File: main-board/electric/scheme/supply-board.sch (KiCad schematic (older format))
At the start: 139 parts, among them K1 CONN_3, P1 PWR-IN, P10 TST, P11 TST, P12 PWR-IN, P13 CONN_4, P14 PWR-IN, P16 TST, P17 TST, P18 TST, P19 TST, P2 PWR-IN, P3 CONN_4, P4 cross board conn, P5 PWR-IN, P6 TST, P7 TST, P8 TST, P9 CONN_3X2, Q1 BC847, Q10 MOS_N, Q11 MOS_P, Q12 MOS_P, Q2 BC847, Q3 BC847, Q4 MOS_P, Q5 BC847, Q6 BC857, Q7 BC847, Q8 BC857, Q9 BC847, U1 NCP3063, U2 L293, U3 MINI-USB-B, X1 8MHz

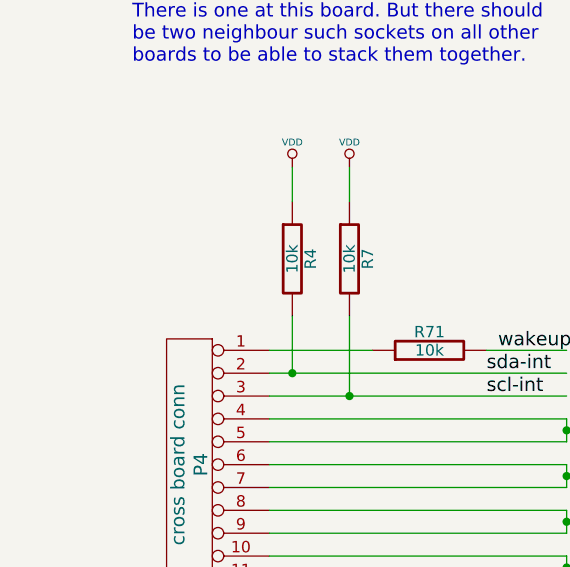
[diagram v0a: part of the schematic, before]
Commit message: Placing elements.
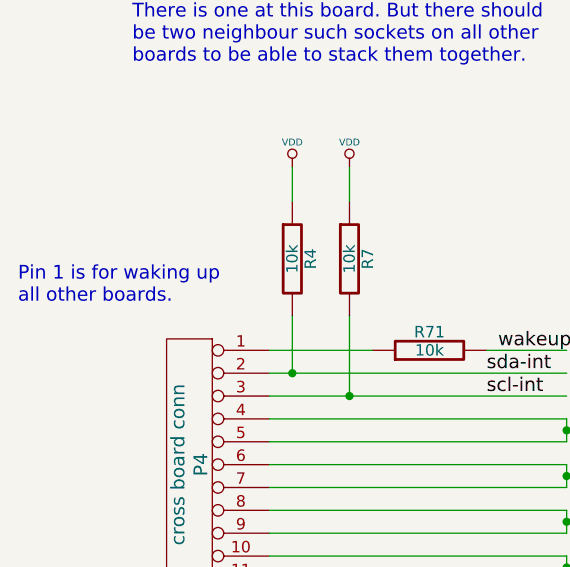
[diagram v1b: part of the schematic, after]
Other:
- note added: "Pin 1 is for waking up \nall other boards."

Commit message: Changed USB power from "batt+" to "solar+".
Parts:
- removed P17, P18, P19: TST, ~, symbol TST
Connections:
- no-connect marks 12 -> 9
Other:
- note added: "Optionally could be USB powered \nthrough "solar+". It is because of \nability to control current through \n"solar+"."
- note removed: "Optionally could be USB powered"
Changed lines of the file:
@@
 Sheet 1 1
 Title ""
-Date "25 aug 2013"
+Date "26 aug 2013"
 Rev ""
 Comp ""
@@
 	29850 18500 29850 17850
 Text Label 29850 18100 1    60   ~ 0
-batt+
-Text Notes 28900 17750 0    60   ~ 0
-Optionally could be USB powered
+solar+
+Text Notes 28850 17500 0    60   ~ 0
+Optionally could be USB powered \nthrough "solar+". It is because of \nability to control current through \n"solar+".
 Text Notes 13550 13400 0    60   ~ 0
 This capacitor gives cutoff frequency at about 170kHz.
@@
 $EndComp
 NoConn ~ 3700 5650
-$Comp
-L TST P17
-U 1 1 5214C655
-P 3950 5650
-F 0 "P17" H 3950 5950 40  0000 C CNN
-F 1 "TST" H 3950 5900 30  0000 C CNN
-F 2 "~" H 3950 5650 60  0000 C CNN
-F 3 "~" H 3950 5650 60  0000 C CNN
-	1    3950 5650
-	1    0    0    -1
-$EndComp
-NoConn ~ 3950 5650
-$Comp
-L TST P18
-U 1 1 5214C65C
-P 4200 5650
-F 0 "P18" H 4200 5950 40  0000 C CNN
-F 1 "TST" H 4200 5900 30  0000 C CNN
-F 2 "~" H 4200 5650 60  0000 C CNN
-F 3 "~" H 4200 5650 60  0000 C CNN
-	1    4200 5650
-	1    0    0    -1
-$EndComp
-NoConn ~ 4200 5650
-$Comp
-L TST P19
-U 1 1 5214C663
-P 4450 5650
-F 0 "P19" H 4450 5950 40  0000 C CNN
-F 1 "TST" H 4450 5900 30  0000 C CNN
-F 2 "~" H 4450 5650 60  0000 C CNN
-F 3 "~" H 4450 5650 60  0000 C CNN
-	1    4450 5650
-	1    0    0    -1
-$EndComp
-NoConn ~ 4450 5650
 Text Notes 3450 5250 0    60   ~ 0
 And four for screws at board corners.

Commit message: Routing...
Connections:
- no-connect marks 9 -> 8
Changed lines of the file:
@@
 Sheet 1 1
 Title ""
-Date "26 aug 2013"
+Date "29 aug 2013"
 Rev ""
 Comp ""
@@
 	1    0    0    -1
 $EndComp
-Text Label 14000 9550 0    60   ~ 0
+Text Label 8400 6350 0    60   ~ 0
 moto4
-Text Label 14000 9750 0    60   ~ 0
+Text Label 8400 7050 0    60   ~ 0
 moto3
 Text Label 13950 8750 0    60   ~ 0
@@
 	1    0    0    -1
 $EndComp
-Text Label 14100 9350 0    60   ~ 0
+Text Label 13950 7950 0    60   ~ 0
 light
 Text Label 23950 16300 0    60   ~ 0
@@
 	0    -1   -1   0
 $EndComp
-Text Label 8400 6350 0    60   ~ 0
+Text Label 14100 9550 0    60   ~ 0
 led1
 Text Label 13950 9150 0    60   ~ 0
@@
 Wire Wire Line
 	9050 7050 8350 7050
-Text Label 8400 7050 0    60   ~ 0
+Text Label 14100 9750 0    60   ~ 0
 led2
-Wire Wire Line
-	13650 6450 14350 6450
-Text Label 14000 6450 0    60   ~ 0
+Text Label 14100 4650 0    60   ~ 0
 usb-connected
 Text Label 14400 5250 0    60   ~ 0
@@
 rx
 NoConn ~ 14500 3050
-NoConn ~ 14500 4650
 $Comp
 L CONN_2 P14
@@
 Text Label 2700 7300 0    60   ~ 0
 wakeup
-NoConn ~ 13650 7950
 Wire Wire Line
 	13650 7600 14300 7600
@@
 Text Notes 600  7100 0    60   ~ 0
 Pin 1 is for waking up \nall other boards.
+NoConn ~ 13650 6450
+Wire Wire Line
+	13650 7950 14300 7950
 $EndSCHEMATC

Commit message: Routing and changing netlist to make routing more convenient.
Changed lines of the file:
@@
 Sheet 1 1
 Title ""
-Date "29 aug 2013"
+Date "30 aug 2013"
 Rev ""
 Comp ""
@@
 Text Label 8400 7050 0    60   ~ 0
 moto3
+Text Label 13950 8550 0    60   ~ 0
+moto2
 Text Label 13950 8750 0    60   ~ 0
-moto2
-Text Label 13950 8550 0    60   ~ 0
 moto1
 Text Label 14100 2750 0    60   ~ 0
@@
 Text Label 22350 12500 0    60   ~ 0
 moto-en
+Text Label 27550 13100 0    60   ~ 0
+out4
+Text Label 27550 13200 0    60   ~ 0
+out3
+Text Label 27550 13400 0    60   ~ 0
+out2
 Text Label 27550 13300 0    60   ~ 0
-out4
-Text Label 27550 13400 0    60   ~ 0
-out3
-Text Label 27550 13100 0    60   ~ 0
-out2
-Text Label 27550 13200 0    60   ~ 0
 out1
 $Comp

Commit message: Routing...
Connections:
- wire segments 412 -> 411
- no-connect marks 8 -> 9
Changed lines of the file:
@@
 Text Label 14000 3250 0    60   ~ 0
 boost-pwm
-Text Label 14100 4050 0    60   ~ 0
+Text Label 14000 3850 0    60   ~ 0
 buck-volt
-Text Label 14100 3850 0    60   ~ 0
+Text Label 14000 3650 0    60   ~ 0
 batt-volt
-Text Label 14100 3650 0    60   ~ 0
+Text Label 14000 4050 0    60   ~ 0
 solar-volt
 Text Label 24150 6550 1    60   ~ 0
@@
 	2450 5000 2900 5000
 Wire Wire Line
-	2900 5100 2450 5100
-Wire Wire Line
 	1650 5100 1150 5100
 Wire Wire Line
@@
 Wire Wire Line
 	2900 5200 2900 5300
-Wire Wire Line
-	2900 4700 2900 5100
-Connection ~ 2900 5000
 Text Label 2100 20950 1    60   ~ 0
 batt+
@@
 Wire Wire Line
 	13650 7950 14300 7950
+Wire Wire Line
+	2900 5000 2900 4350
+NoConn ~ 2450 5100
 $EndSCHEMATC

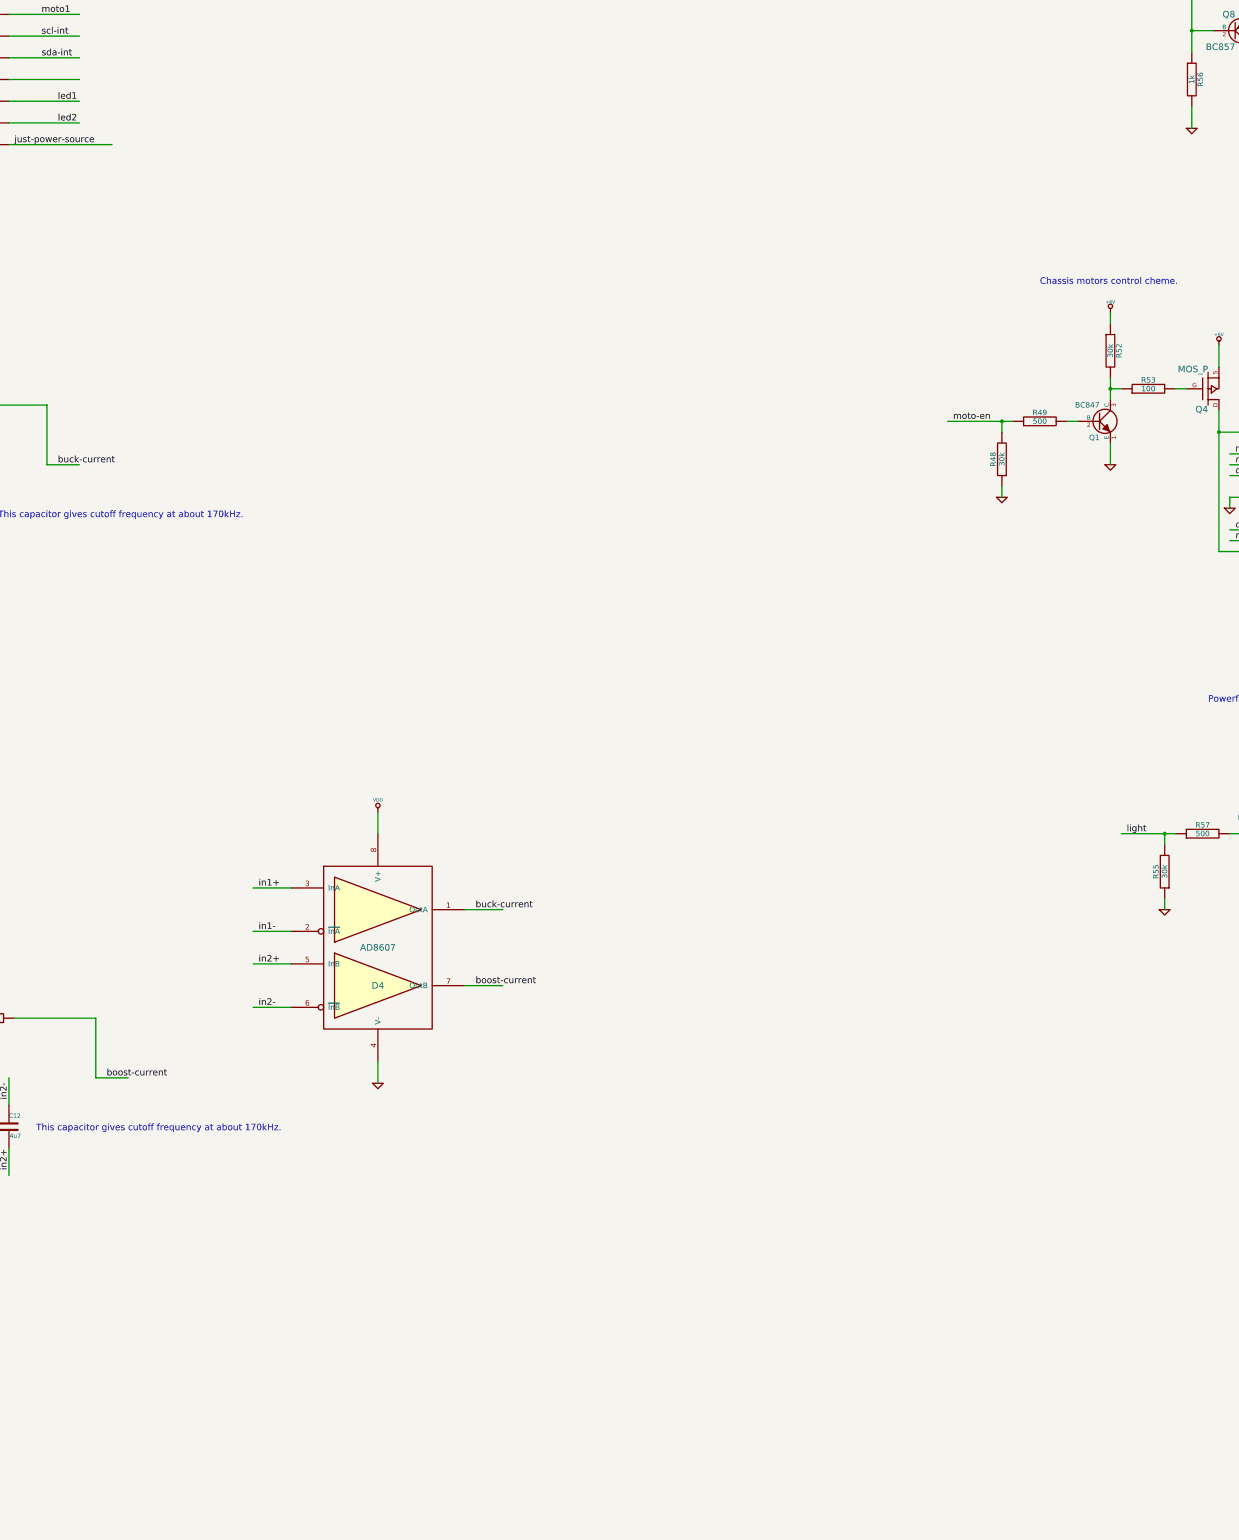
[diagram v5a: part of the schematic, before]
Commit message: Added acelerometer (it's optional).
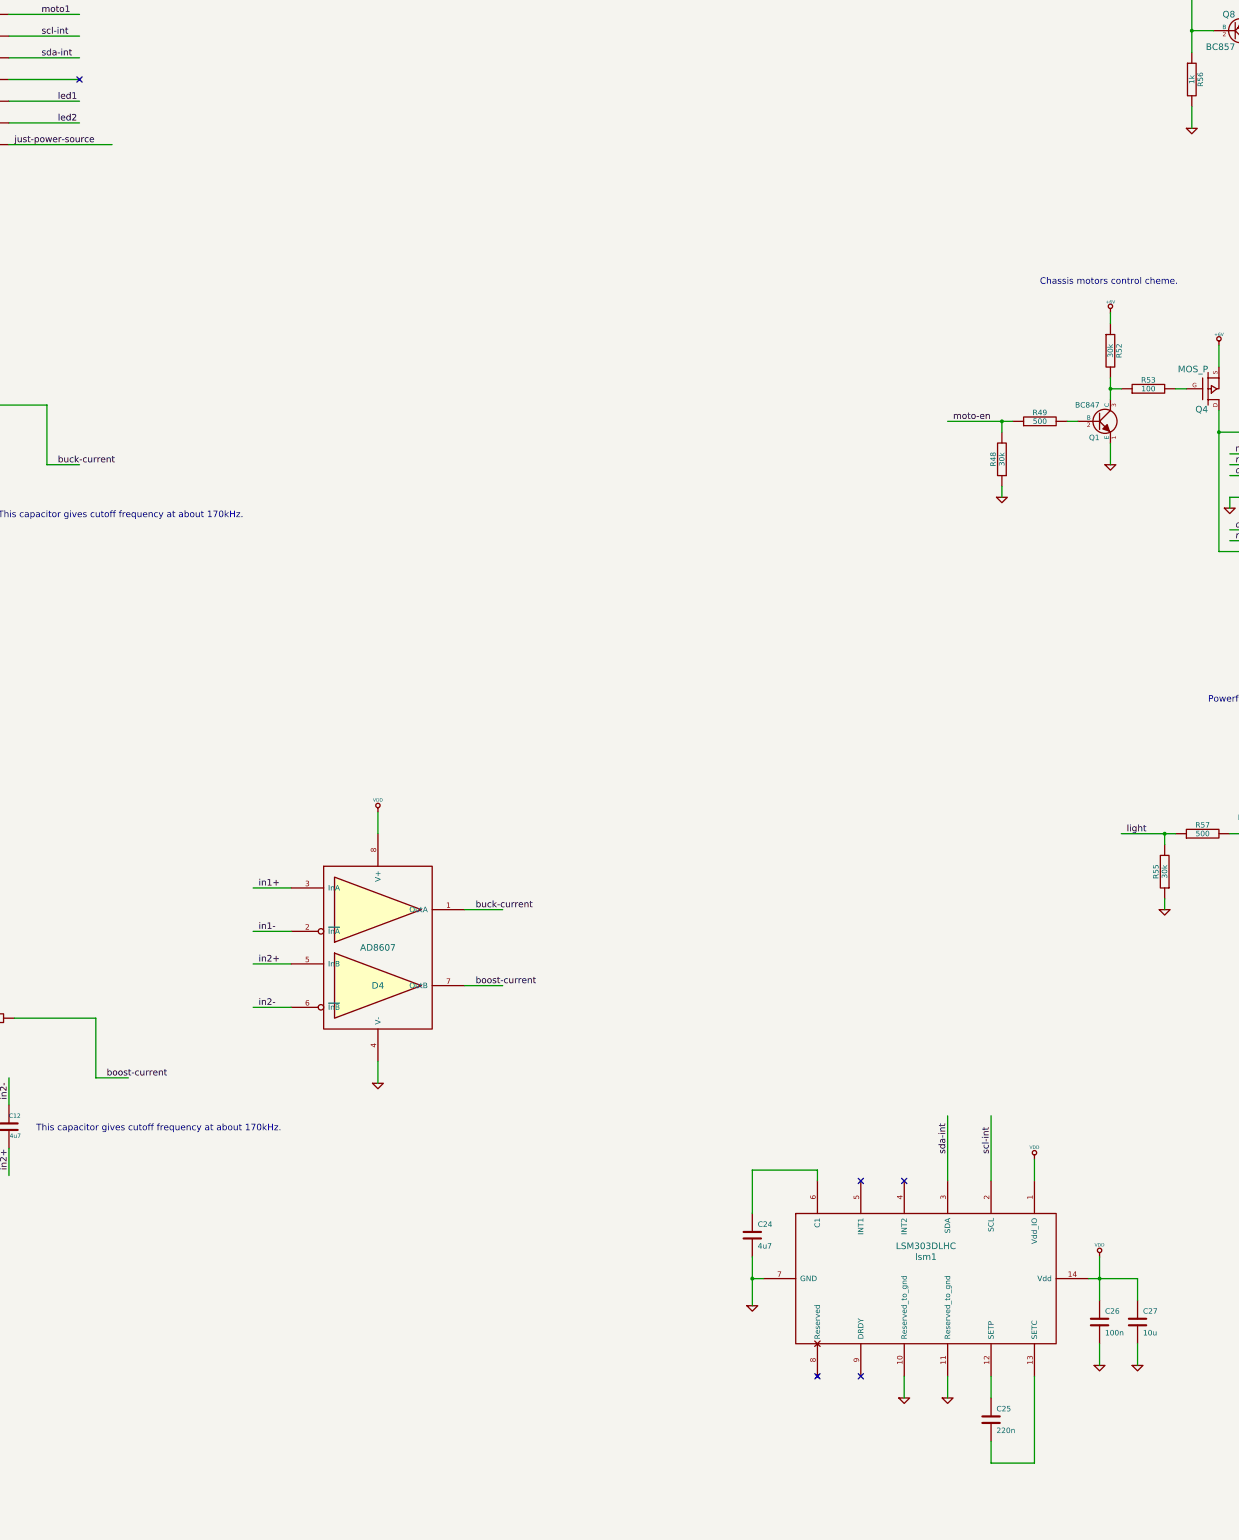
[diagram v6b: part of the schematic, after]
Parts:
- added C24: 4u7, symbol C
- added C25: 220n, symbol C
- added C26: 100n, symbol C
- added C27: 10u, symbol C
- added lsm1: LSM303DLHC, symbol LSM303DLHC
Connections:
- wire segments 411 -> 430
- no-connect marks 9 -> 14
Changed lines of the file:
@@
 Sheet 1 1
 Title ""
-Date "30 aug 2013"
+Date "31 aug 2013"
 Rev ""
 Comp ""
@@
 	2900 5000 2900 4350
 NoConn ~ 2450 5100
+Wire Wire Line
+	22300 19500 22300 18900
+Wire Wire Line
+	24050 21000 24050 21200
+Connection ~ 23700 20400
+Wire Wire Line
+	23600 20400 24050 20400
+Wire Wire Line
+	24050 20400 24050 20600
+Wire Wire Line
+	23100 19500 23100 19300
+Wire Wire Line
+	22700 21300 22700 21500
+Connection ~ 20500 20400
+Wire Wire Line
+	20500 20650 20500 20200
+Wire Wire Line
+	20500 19800 20500 19400
+Wire Wire Line
+	20500 19400 21100 19400
+Wire Wire Line
+	21100 19400 21100 19500
+Wire Wire Line
+	20500 20400 20600 20400
+Wire Wire Line
+	22300 21300 22300 21500
+Wire Wire Line
+	21900 21300 21900 21500
+Wire Wire Line
+	22700 21900 22700 22100
+Wire Wire Line
+	22700 22100 23100 22100
+Wire Wire Line
+	23100 22100 23100 21300
+Wire Wire Line
+	23700 21000 23700 21200
+Wire Wire Line
+	23700 20200 23700 20600
+Wire Wire Line
+	22700 18900 22700 19500
+$Comp
+L LSM303DLHC lsm1
+U 1 1 52220512
+P 22100 20400
+F 0 "lsm1" H 22100 20600 60  0000 C CNN
+F 1 "LSM303DLHC" H 22100 20700 60  0000 C CNN
+F 2 "" H 22100 20400 60  0001 C CNN
+F 3 "" H 22100 20400 60  0001 C CNN
+	1    22100 20400
+	1    0    0    -1
+$EndComp
+$Comp
+L C C24
+U 1 1 52220518
+P 20500 20000
+F 0 "C24" H 20550 20100 50  0000 L CNN
+F 1 "4u7" H 20550 19900 50  0000 L CNN
+F 2 "" H 20500 20000 60  0001 C CNN
+F 3 "" H 20500 20000 60  0001 C CNN
+	1    20500 20000
+	1    0    0    -1
+$EndComp
+$Comp
+L C C27
+U 1 1 5222051E
+P 24050 20800
+F 0 "C27" H 24100 20900 50  0000 L CNN
+F 1 "10u" H 24100 20700 50  0000 L CNN
+F 2 "" H 24050 20800 60  0001 C CNN
+F 3 "" H 24050 20800 60  0001 C CNN
+	1    24050 20800
+	1    0    0    -1
+$EndComp
+$Comp
+L C C26
+U 1 1 52220524
+P 23700 20800
+F 0 "C26" H 23750 20900 50  0000 L CNN
+F 1 "100n" H 23750 20700 50  0000 L CNN
+F 2 "" H 23700 20800 60  0001 C CNN
+F 3 "" H 23700 20800 60  0001 C CNN
+	1    23700 20800
+	1    0    0    -1
+$EndComp
+NoConn ~ 21500 19500
+NoConn ~ 21900 19500
+NoConn ~ 21500 21300
+NoConn ~ 21100 21300
+$Comp
+L C C25
+U 1 1 5222052E
+P 22700 21700
+F 0 "C25" H 22750 21800 50  0000 L CNN
+F 1 "220n" H 22750 21600 50  0000 L CNN
+F 2 "" H 22700 21700 60  0001 C CNN
+F 3 "" H 22700 21700 60  0001 C CNN
+	1    22700 21700
+	1    0    0    -1
+$EndComp
+$Comp
+L GND #PWR090
+U 1 1 52220534
+P 20500 20650
+F 0 "#PWR090" H 20500 20650 30  0001 C CNN
+F 1 "GND" H 20500 20580 30  0001 C CNN
+F 2 "" H 20500 20650 60  0001 C CNN
+F 3 "" H 20500 20650 60  0001 C CNN
+	1    20500 20650
+	1    0    0    -1
+$EndComp
+$Comp
+L GND #PWR091
+U 1 1 5222053A
+P 22300 21500
+F 0 "#PWR091" H 22300 21500 30  0001 C CNN
+F 1 "GND" H 22300 21430 30  0001 C CNN
+F 2 "" H 22300 21500 60  0001 C CNN
+F 3 "" H 22300 21500 60  0001 C CNN
+	1    22300 21500
+	1    0    0    -1
+$EndComp
+$Comp
+L GND #PWR092
+U 1 1 52220540
+P 21900 21500
+F 0 "#PWR092" H 21900 21500 30  0001 C CNN
+F 1 "GND" H 21900 21430 30  0001 C CNN
+F 2 "" H 21900 21500 60  0001 C CNN
+F 3 "" H 21900 21500 60  0001 C CNN
+	1    21900 21500
+	1    0    0    -1
+$EndComp
+$Comp
+L VDD #PWR093
+U 1 1 52220546
+P 23100 19300
+F 0 "#PWR093" H 23100 19400 30  0001 C CNN
+F 1 "VDD" H 23100 19410 30  0000 C CNN
+F 2 "" H 23100 19300 60  0001 C CNN
+F 3 "" H 23100 19300 60  0001 C CNN
+	1    23100 19300
+	1    0    0    -1
+$EndComp
+$Comp
+L GND #PWR094
+U 1 1 5222054C
+P 23700 21200
+F 0 "#PWR094" H 23700 21200 30  0001 C CNN
+F 1 "GND" H 23700 21130 30  0001 C CNN
+F 2 "" H 23700 21200 60  0001 C CNN
+F 3 "" H 23700 21200 60  0001 C CNN
+	1    23700 21200
+	1    0    0    -1
+$EndComp
+$Comp
+L GND #PWR095
+U 1 1 52220552
+P 24050 21200
+F 0 "#PWR095" H 24050 21200 30  0001 C CNN
+F 1 "GND" H 24050 21130 30  0001 C CNN
+F 2 "" H 24050 21200 60  0001 C CNN
+F 3 "" H 24050 21200 60  0001 C CNN
+	1    24050 21200
+	1    0    0    -1
+$EndComp
+$Comp
+L VDD #PWR096
+U 1 1 52220558
+P 23700 20200
+F 0 "#PWR096" H 23700 20300 30  0001 C CNN
+F 1 "VDD" H 23700 20310 30  0000 C CNN
+F 2 "" H 23700 20200 60  0001 C CNN
+F 3 "" H 23700 20200 60  0001 C CNN
+	1    23700 20200
+	1    0    0    -1
+$EndComp
+Text Label 22300 19250 1    60   ~ 0
+sda-int
+Text Label 22700 19250 1    60   ~ 0
+scl-int
+NoConn ~ 14300 9350
 $EndSCHEMATC

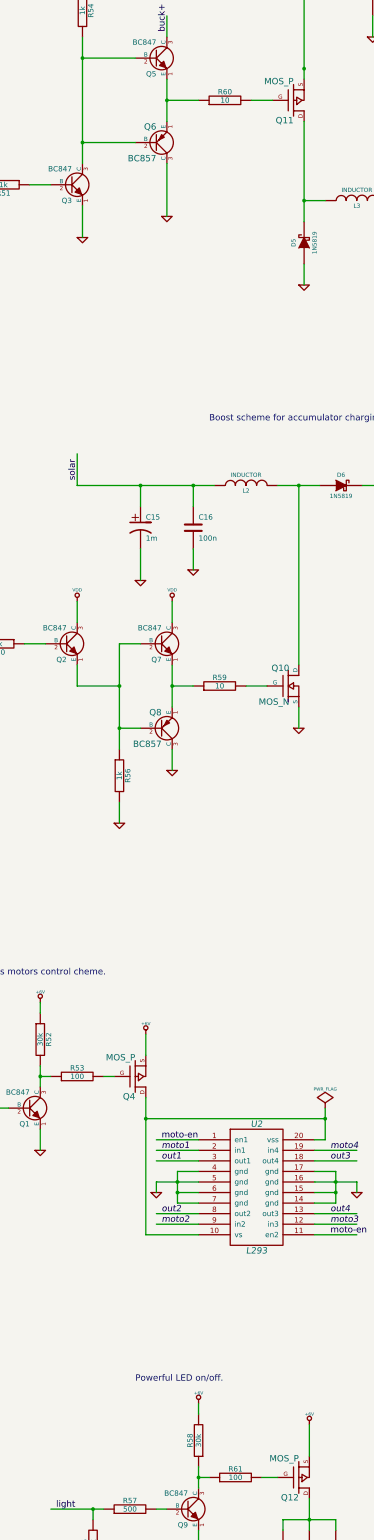
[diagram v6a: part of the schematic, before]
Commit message: Raplaced power mosfets with sot23 transistors because of their max current and very low resistance.
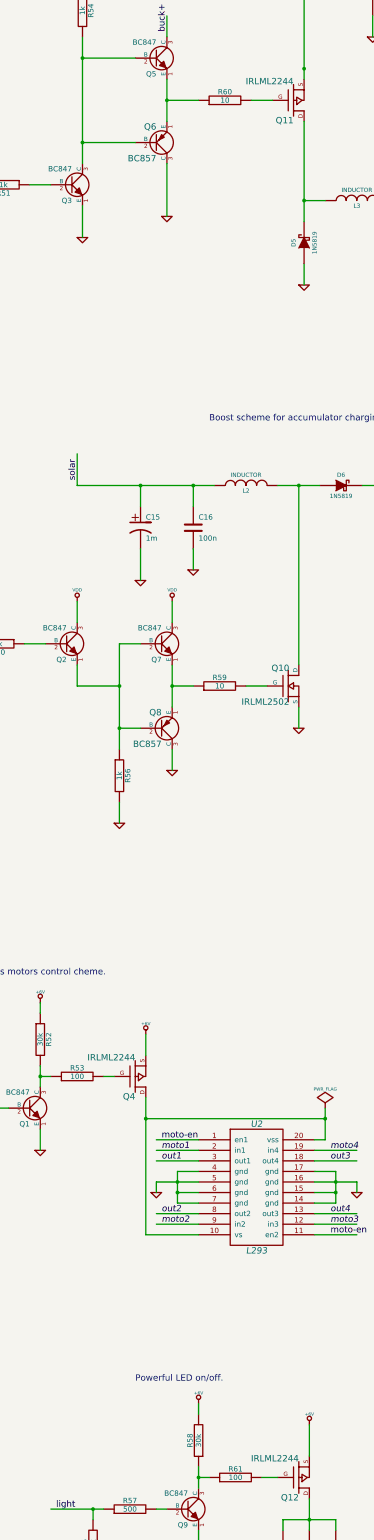
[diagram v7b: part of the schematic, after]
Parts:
- Q10: value MOS_N -> IRLML2502
- Q11, Q12, Q4: value MOS_P -> IRLML2244
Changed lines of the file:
@@
 Sheet 1 1
 Title ""
-Date "31 aug 2013"
+Date "10 sep 2013"
 Rev ""
 Comp ""
@@
 P 24700 12200
 F 0 "Q4" H 24700 12390 60  0000 R CNN
-F 1 "MOS_P" H 24700 12020 60  0000 R CNN
+F 1 "IRLML2244" H 24700 12020 60  0000 R CNN
 F 2 "" H 24700 12200 60  0001 C CNN
 F 3 "" H 24700 12200 60  0001 C CNN
@@
 P 26250 16000
 F 0 "Q12" H 26250 16190 60  0000 R CNN
-F 1 "MOS_P" H 26250 15820 60  0000 R CNN
+F 1 "IRLML2244" H 26250 15820 60  0000 R CNN
 F 2 "" H 26250 16000 60  0001 C CNN
 F 3 "" H 26250 16000 60  0001 C CNN
@@
 P 26200 2950
 F 0 "Q11" H 26200 3140 60  0000 R CNN
-F 1 "MOS_P" H 26200 2770 60  0000 R CNN
+F 1 "IRLML2244" H 26200 2770 60  0000 R CNN
 F 2 "" H 26200 2950 60  0001 C CNN
 F 3 "" H 26200 2950 60  0001 C CNN
@@
 P 26150 8500
 F 0 "Q10" H 26160 8670 60  0000 R CNN
-F 1 "MOS_N" H 26160 8350 60  0000 R CNN
+F 1 "IRLML2502" H 26160 8350 60  0000 R CNN
 F 2 "" H 26150 8500 60  0001 C CNN
 F 3 "" H 26150 8500 60  0001 C CNN
